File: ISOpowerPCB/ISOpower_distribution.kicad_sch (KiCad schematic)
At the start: 28 parts

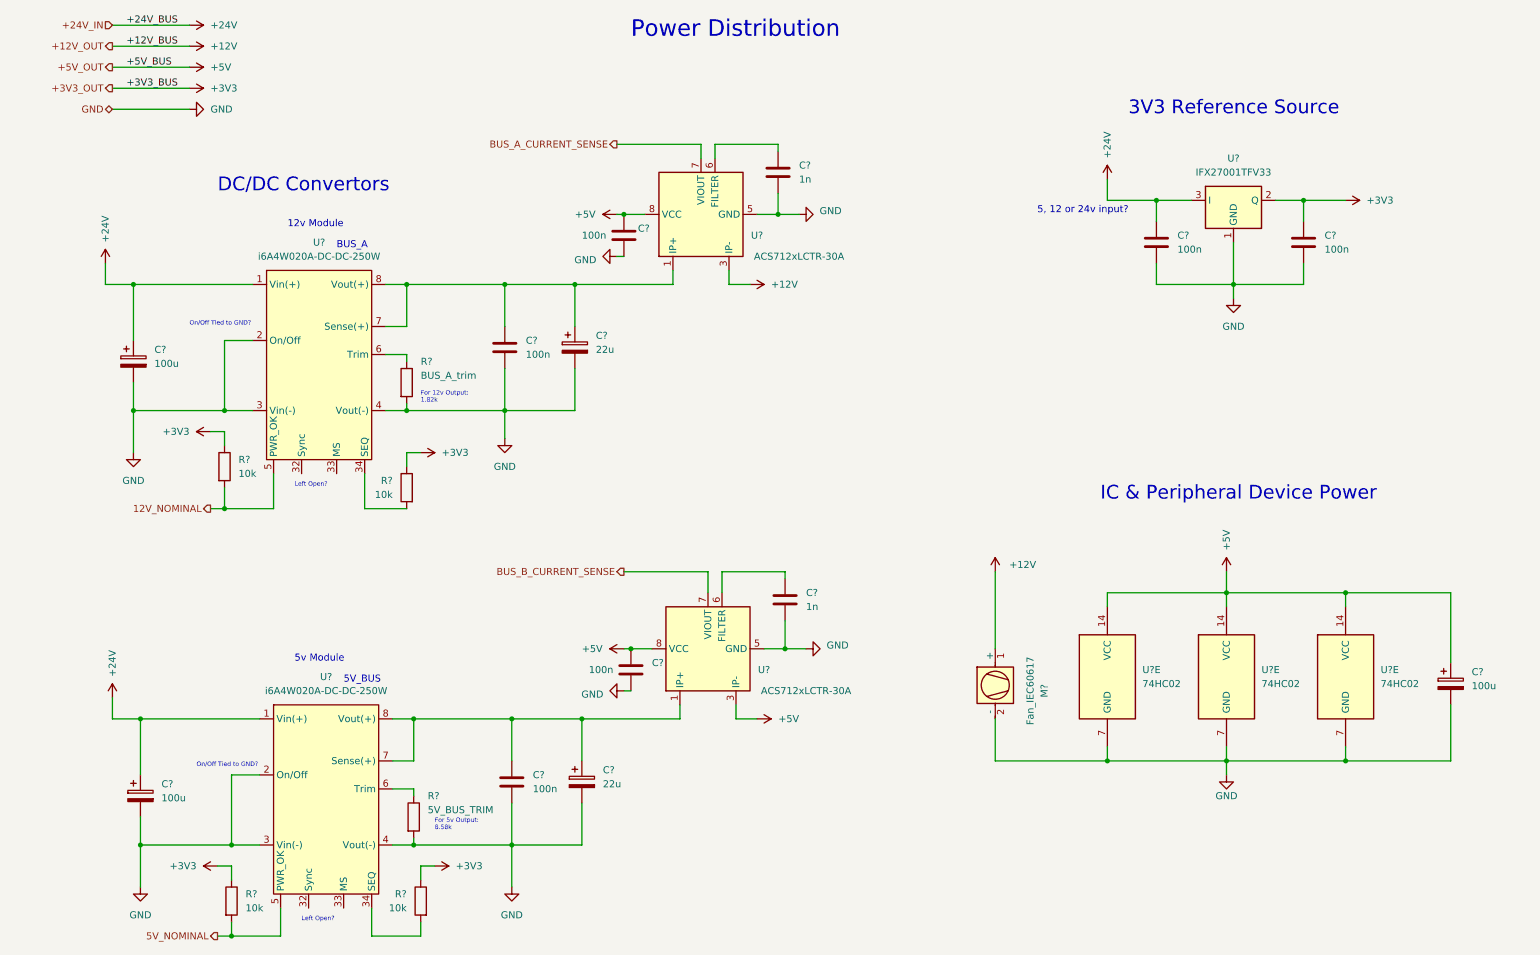
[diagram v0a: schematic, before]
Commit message: Finished initial circuit design
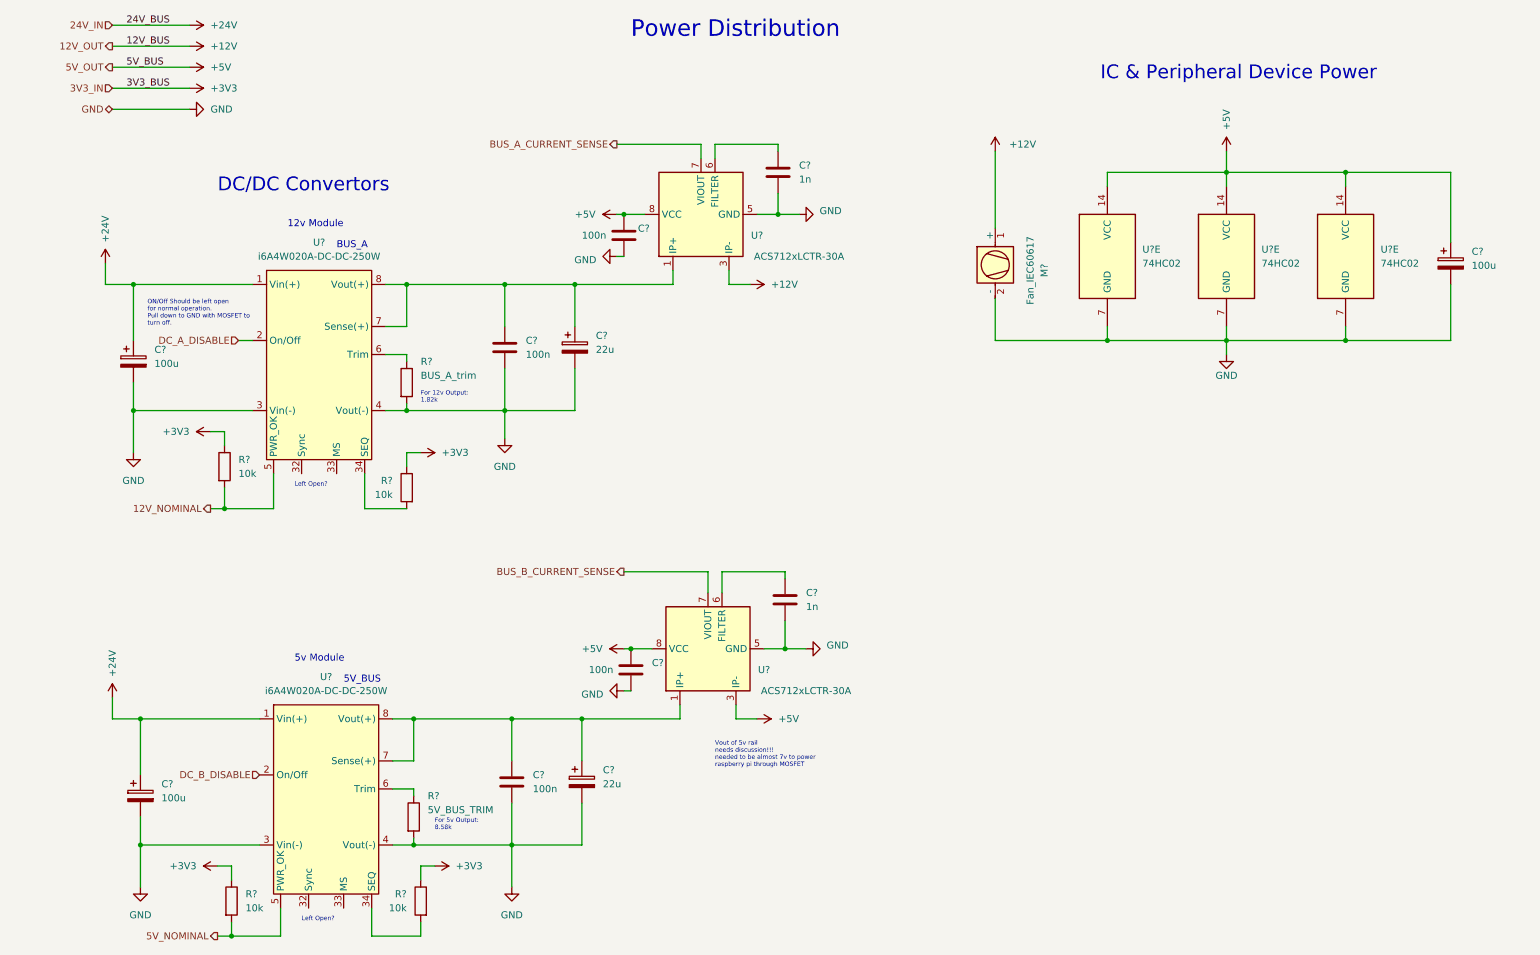
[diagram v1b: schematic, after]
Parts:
- removed C? (x2): 100n, Capacitor_SMD:C_0805_2012Metric_Pad1.18x1.45mm_HandSolder, symbol 000_Capacitor_film_immo:cap_film_0805
- removed U?: IFX27001TFV33, Package_TO_SOT_SMD:TO-252-3_TabPin2, symbol Regulator_Linear:IFX27001TFV33
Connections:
- net GND: no longer U?.2 (On/Off), U?.2 (On/Off)
- new net DC_A_DISABLE: U?.2 (On/Off)
- new net DC_B_DISABLE: U?.2 (On/Off)
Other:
- note added: "ON/Off Should be left open for normal operation. Pull down to GND with MOSFET to turn off."
- note added: "Vout of 5v rail needs discussion!!! needed to be almost 7v to power raspberry pi through MOSFET"
- note removed: "3V3 Reference Source"
- note removed: "5, 12 or 24v input?"
- note removed: "On/Off Tied to GND?"
- moved on the sheet: C?, M?, U?E

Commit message: PCB Notes added
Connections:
- net DC_A_DISABLE is gone; now on net GND: U?.2 (On/Off)
- net DC_B_DISABLE is gone; now on net GND: U?.2 (On/Off)
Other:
- note added: "NOTE: THESE PINS DONT EXIST"
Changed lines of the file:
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@@
   (junction (at 228.6 74.93) (diameter 0) (color 0 0 0 0)
   )
+  (junction (at 45.72 166.37) (diameter 0) (color 0 0 0 0)
+  )
   (junction (at 119.38 52.07) (diameter 0) (color 0 0 0 0)
   )
@@
   (junction (at 99.06 143.51) (diameter 0) (color 0 0 0 0)
   )
+  (junction (at 45.72 87.63) (diameter 0) (color 0 0 0 0)
+  )
   (junction (at 110.49 64.77) (diameter 0) (color 0 0 0 0)
   )
@@
     (stroke (width 0) (type default) (color 0 0 0 0))
   )
+  (wire (pts (xy 45.72 87.63) (xy 52.07 87.63))
+    (stroke (width 0) (type default) (color 0 0 0 0))
+  )
   (wire (pts (xy 77.47 151.13) (xy 81.28 151.13))
     (stroke (width 0) (type default) (color 0 0 0 0))
@@
     (stroke (width 0) (type default) (color 0 0 0 0))
   )
+  (polyline (pts (xy 95.25 90.17) (xy 35.56 90.17))
+    (stroke (width 0) (type default) (color 0 0 0 0))
+  )
   (wire (pts (xy 99.06 166.37) (xy 111.76 166.37))
     (stroke (width 0) (type default) (color 0 0 0 0))
@@
     (stroke (width 0) (type default) (color 0 0 0 0))
   )
-  (wire (pts (xy 49.53 74.93) (xy 52.07 74.93))
+  (wire (pts (xy 45.72 74.93) (xy 52.07 74.93))
+    (stroke (width 0) (type default) (color 0 0 0 0))
+  )
+  (wire (pts (xy 45.72 153.67) (xy 45.72 166.37))
     (stroke (width 0) (type default) (color 0 0 0 0))
   )
@@
     (stroke (width 0) (type default) (color 0 0 0 0))
   )
+  (wire (pts (xy 53.34 153.67) (xy 45.72 153.67))
+    (stroke (width 0) (type default) (color 0 0 0 0))
+  )
   (wire (pts (xy 26.67 25.4) (xy 40.64 25.4))
     (stroke (width 0) (type default) (color 0 0 0 0))
@@
     (stroke (width 0) (type default) (color 0 0 0 0))
   )
+  (polyline (pts (xy 95.25 109.22) (xy 95.25 90.17))
+    (stroke (width 0) (type default) (color 0 0 0 0))
+  )
   (wire (pts (xy 269.24 74.93) (xy 269.24 64.77))
     (stroke (width 0) (type default) (color 0 0 0 0))
@@
     (stroke (width 0) (type default) (color 0 0 0 0))
   )
-  (wire (pts (xy 31.75 166.37) (xy 53.34 166.37))
+  (wire (pts (xy 31.75 166.37) (xy 45.72 166.37))
     (stroke (width 0) (type default) (color 0 0 0 0))
   )
@@
     (stroke (width 0) (type default) (color 0 0 0 0))
   )
+  (wire (pts (xy 45.72 74.93) (xy 45.72 87.63))
+    (stroke (width 0) (type default) (color 0 0 0 0))
+  )
   (wire (pts (xy 26.67 143.51) (xy 31.75 143.51))
     (stroke (width 0) (type default) (color 0 0 0 0))
@@
     (stroke (width 0) (type default) (color 0 0 0 0))
   )
+  (polyline (pts (xy 35.56 88.9) (xy 35.56 90.17))
+    (stroke (width 0) (type default) (color 0 0 0 0))
+  )
   (wire (pts (xy 148.59 116.84) (xy 137.16 116.84))
     (stroke (width 0) (type default) (color 0 0 0 0))
@@
     (stroke (width 0) (type default) (color 0 0 0 0))
   )
+  (polyline (pts (xy 35.56 88.9) (xy 35.56 109.22))
+    (stroke (width 0) (type default) (color 0 0 0 0))
+  )
   (wire (pts (xy 120.65 130.81) (xy 124.46 130.81))
     (stroke (width 0) (type default) (color 0 0 0 0))
@@
     (stroke (width 0) (type default) (color 0 0 0 0))
   )
+  (wire (pts (xy 45.72 166.37) (xy 53.34 166.37))
+    (stroke (width 0) (type default) (color 0 0 0 0))
+  )
   (wire (pts (xy 97.79 72.39) (xy 97.79 64.77))
     (stroke (width 0) (type default) (color 0 0 0 0))
@@
     (stroke (width 0) (type default) (color 0 0 0 0))
   )
-  (wire (pts (xy 30.48 87.63) (xy 52.07 87.63))
+  (wire (pts (xy 30.48 87.63) (xy 45.72 87.63))
     (stroke (width 0) (type default) (color 0 0 0 0))
   )
@@
   )
   (wire (pts (xy 119.38 116.84) (xy 134.62 116.84))
+    (stroke (width 0) (type default) (color 0 0 0 0))
+  )
+  (polyline (pts (xy 35.56 109.22) (xy 95.25 109.22))
     (stroke (width 0) (type default) (color 0 0 0 0))
   )
@@
     (effects (font (size 2.5 2.5)) (justify left bottom))
   )
-  (text "Left Open?" (at 59.69 101.6 0)
+  (text "NOTE: THESE PINS DONT EXIST" (at 52.07 109.22 0)
     (effects (font (size 0.8 0.8)) (justify left bottom))
   )
@@
     (effects (font (size 2.5 2.5)) (justify left bottom))
   )
-  (text "For 12v Output:\n1.82k" (at 82.55 86.36 0)
+  (text "For 12v Output:\n1.82k" (at 81.28 86.36 0)
     (effects (font (size 0.8 0.8)) (justify left bottom))
   )
@@
   )
   (hierarchical_label "12V_OUT" (shape output) (at 26.67 21.59 180)
-    (effects (font (size 1.27 1.27)) (justify right))
-  )
-  (hierarchical_label "DC_A_DISABLE" (shape input) (at 49.53 74.93 180)
-    (effects (font (size 1.27 1.27)) (justify right))
-  )
-  (hierarchical_label "DC_B_DISABLE" (shape input) (at 53.34 153.67 180)
     (effects (font (size 1.27 1.27)) (justify right))
   )
@@
   (symbol (lib_id "000_Resistors_Immo:Resistor_0805") (at 80.01 82.55 0) (unit 1)
     (in_bom yes) (on_board yes)
-    (property "Reference" "R?" (id 0) (at 82.55 78.74 0)
-      (effects (font (size 1.27 1.27)) (justify left))
-    )
-    (property "Value" "BUS_A_trim" (id 1) (at 82.55 81.28 0)
-      (effects (font (size 1.27 1.27)) (justify left))
-    )
+    (property "Reference" "R?" (id 0) (at 80.01 73.66 0)
+      (effects (font (size 1.27 1.27)) (justify left))
+    )
+    (property "Value" "BUS_A_trim" (id 1) (at 80.01 76.2 0)
+      (effects (font (size 1.27 1.27)) (justify left))
+    )

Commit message: Major schematic revisions
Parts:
- removed R? (x4): 10k, Resistor_SMD:R_0805_2012Metric_Pad1.20x1.40mm_HandSolder, symbol 000_Resistors_Immo:Resistor_0805
- added C?: 220u, Capacitor_SMD:CP_Elec_10x10, symbol 000_Capacitor_electrolytic_immo:100u
- added C?: 680u, Capacitor_SMD:CP_Elec_10x10, symbol 000_Capacitor_electrolytic_immo:100u
- added D?: 1N5821, Diode_THT:D_DO-201AD_P15.24mm_Horizontal, symbol Diode:1N5821
- added L?: 33uH, symbol Device:L
- added Q? (x2): IRF5305_PBF, Package_TO_SOT_THT:TO-220-3_Vertical, symbol 000_MOSFET_Immo:IRF5305_PBF
- added U?: LM2596S-5, Package_TO_SOT_SMD:TO-263-5_TabPin3, symbol Regulator_Switching:LM2596S-5
- M?: footprint (none) -> Fuse:Fuseholder_Keystone_3555-2
- U? (x2): footprint (none) -> ISOpower:i6A4W-DIP
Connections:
- net +24V: now also C?.1, U?.1 (VIN)
- net GND: now also C?.2, C?.2, D?.2 (A), Q?.2 (D), Q?.2 (D), U?.3 (GND), U?.5 (~{ON}/OFF); no longer U?.2 (On/Off), U?.2 (On/Off)
- net 12V_NOMINAL: no longer names the net of U?.5 (PWR_OK)
- net 5V_NOMINAL: no longer names the net of U?.5 (PWR_OK)
- new net: Q?.3 (S), U?.2 (On/Off) (x2)
- new net: D?.1 (K), L?.1, U?.2 (OUT)
- new net BUS_A_DISABLE: Q?.1 (G)
- new net BUS_B_DISABLE: Q?.1 (G)
- new net MCU_5V_OUT: C?.1, L?.2, U?.4 (FB)
- no-connect marks 0 -> 8
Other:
- note added: "5vDC Buck Converter"
- note added: "DC/DC Converters"
- note added: "NOTE: THESE PINS DON'T EXIST"
- note removed: "DC/DC Convertors"
- note removed: "Left Open?"
- note removed: "NOTE: THESE PINS DONT EXIST"
- note removed: "ON/Off Should be left open for normal operation. Pull down to GND with MOSFET to turn off."
- note removed: "Vout of 5v rail needs discussion!!! needed to be almost 7v to power raspberry pi through MOSFET"
- moved on the sheet: C?, R?, U?
